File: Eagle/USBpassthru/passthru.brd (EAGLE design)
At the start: 17.1 x 17.1 mm, 4 parts

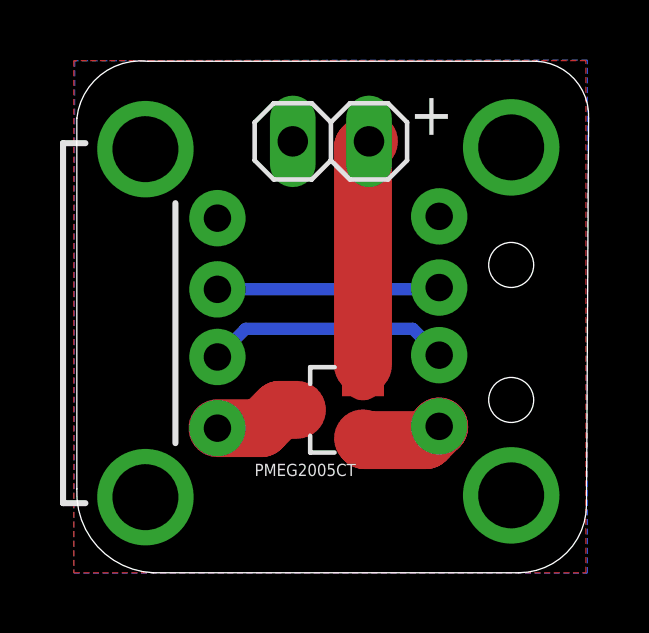
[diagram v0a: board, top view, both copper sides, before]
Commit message: Add new package and wire connections in pasthru.brd
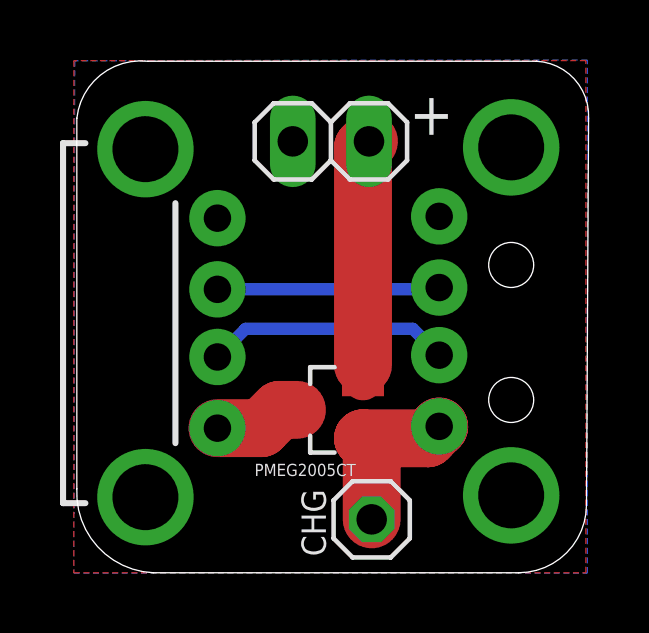
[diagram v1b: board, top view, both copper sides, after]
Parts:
- added CHG: (no value), pinhead:1X01
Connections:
- net +5V: now also CHG.1
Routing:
- net +5V: track 2.76 -> 5.53 mm
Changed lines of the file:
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@@
 <attribute name="VALUE" x="11.11" y="17.555" size="1.27" layer="27" rot="R180"/>
+</element>
+<element name="CHG" library="pinhead" library_urn="urn:adsk.eagle:library:325" package="1X01" package3d_urn="urn:adsk.eagle:package:22485/2" value="" x="9.93" y="1.78" smashed="yes">
+<attribute name="NAME" x="8.4038" y="0.5488" size="0.8128" layer="25" font="vector" ratio="10" rot="R90"/>
+<attribute name="POPULARITY" value="64" x="9.93" y="1.78" size="1.778" layer="27" ratio="12" display="off"/>
+<attribute name="VALUE" x="8.66" y="-1.395" size="1.27" layer="27"/>
 </element>
 </elements>
@@
 <contactref element="IN" pad="VBUS"/>
 <contactref element="PMEG2005CT" pad="1"/>
-<wire x1="9.64" y1="4.48" x2="9.6984" y2="4.4216" width="1.9304" layer="1"/>
-<wire x1="9.6984" y1="4.4216" x2="11.73396875" y2="4.4216" width="1.9304" layer="1"/>
+<wire x1="11.79396875" y1="4.4816" x2="9.6416" y2="4.4816" width="1.9304" layer="1"/>
+<wire x1="9.64" y1="4.48" x2="9.6416" y2="4.4816" width="1.9304" layer="1"/>
 <wire x1="12.18" y1="4.88" x2="12.18" y2="4.86763125" width="1.9304" layer="1"/>
-<wire x1="12.18" y1="4.86763125" x2="11.73396875" y2="4.4216" width="1.9304" layer="1"/>
+<wire x1="12.18" y1="4.86763125" x2="11.79396875" y2="4.4816" width="1.9304" layer="1"/>
+<contactref element="CHG" pad="1"/>
+<wire x1="9.93" y1="1.78" x2="9.93" y2="4.1932" width="1.9304" layer="1"/>
+<wire x1="9.93" y1="4.1932" x2="9.6416" y2="4.4816" width="1.9304" layer="1"/>
 </signal>
 <signal name="GND">
